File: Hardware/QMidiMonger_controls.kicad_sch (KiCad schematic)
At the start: 26 parts, among them J1 CV_Out, J10 Conn_01x04, J2 CV_Out, J20 Conn_01x09_Female, J21 Conn_01x08_Female, J22 Conn_01x08_Female, J23 Conn_01x03_Female, J3 CV_Out, J4 Gate_Out, J5 Gate_Out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

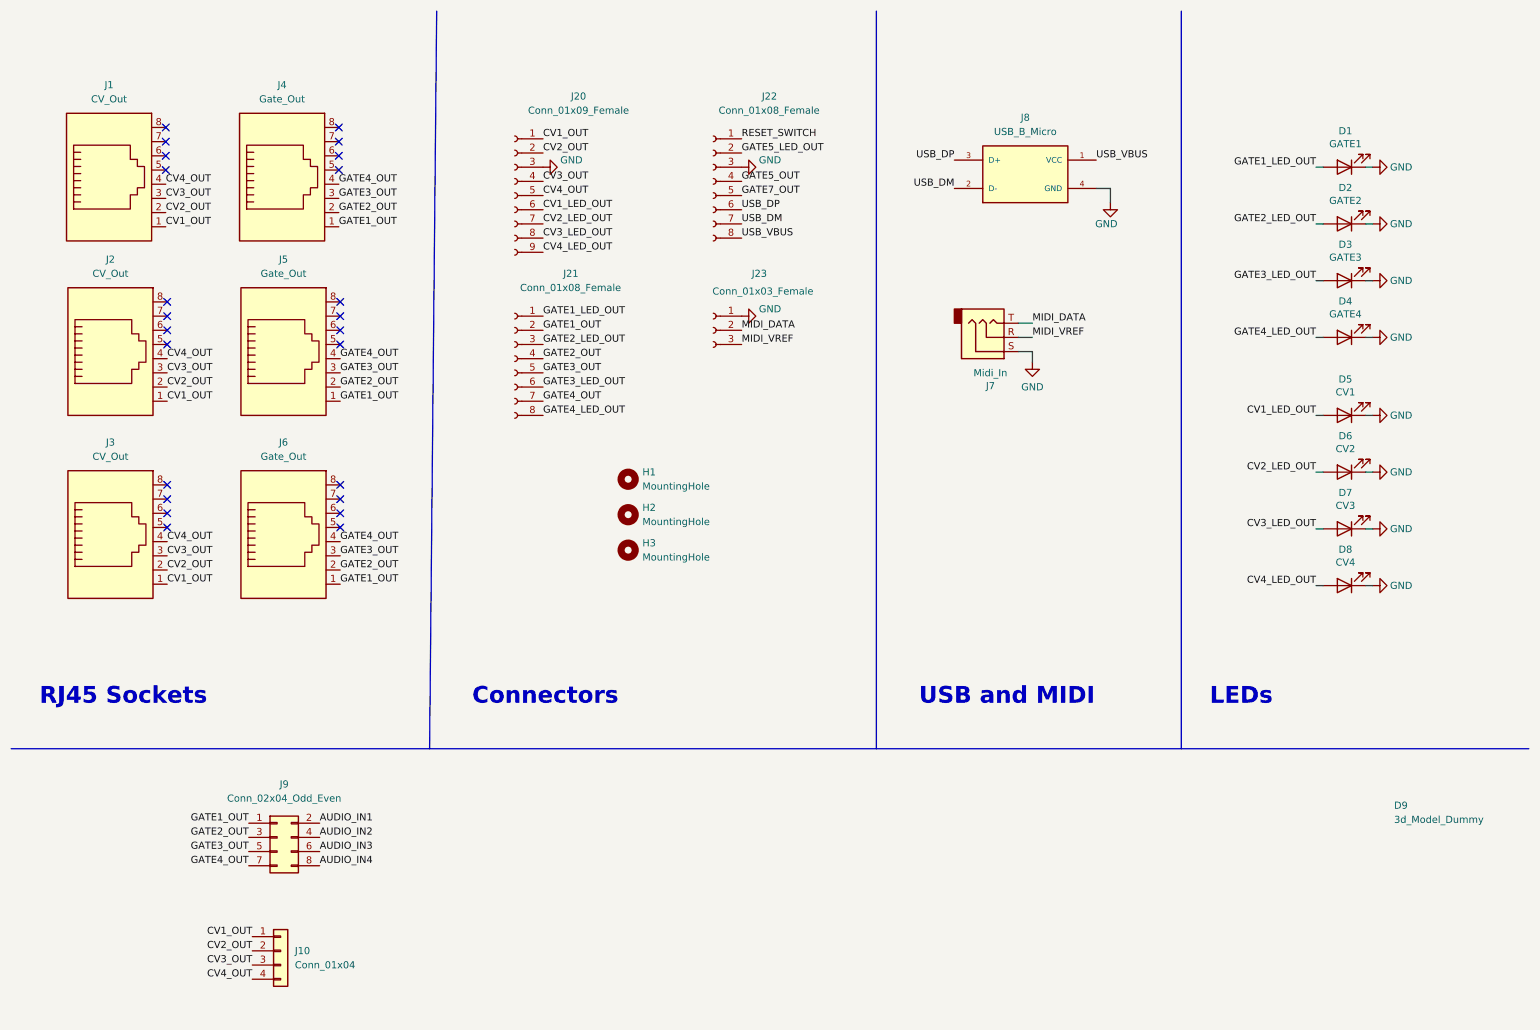
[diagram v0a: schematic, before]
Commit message: Added inter-board connector
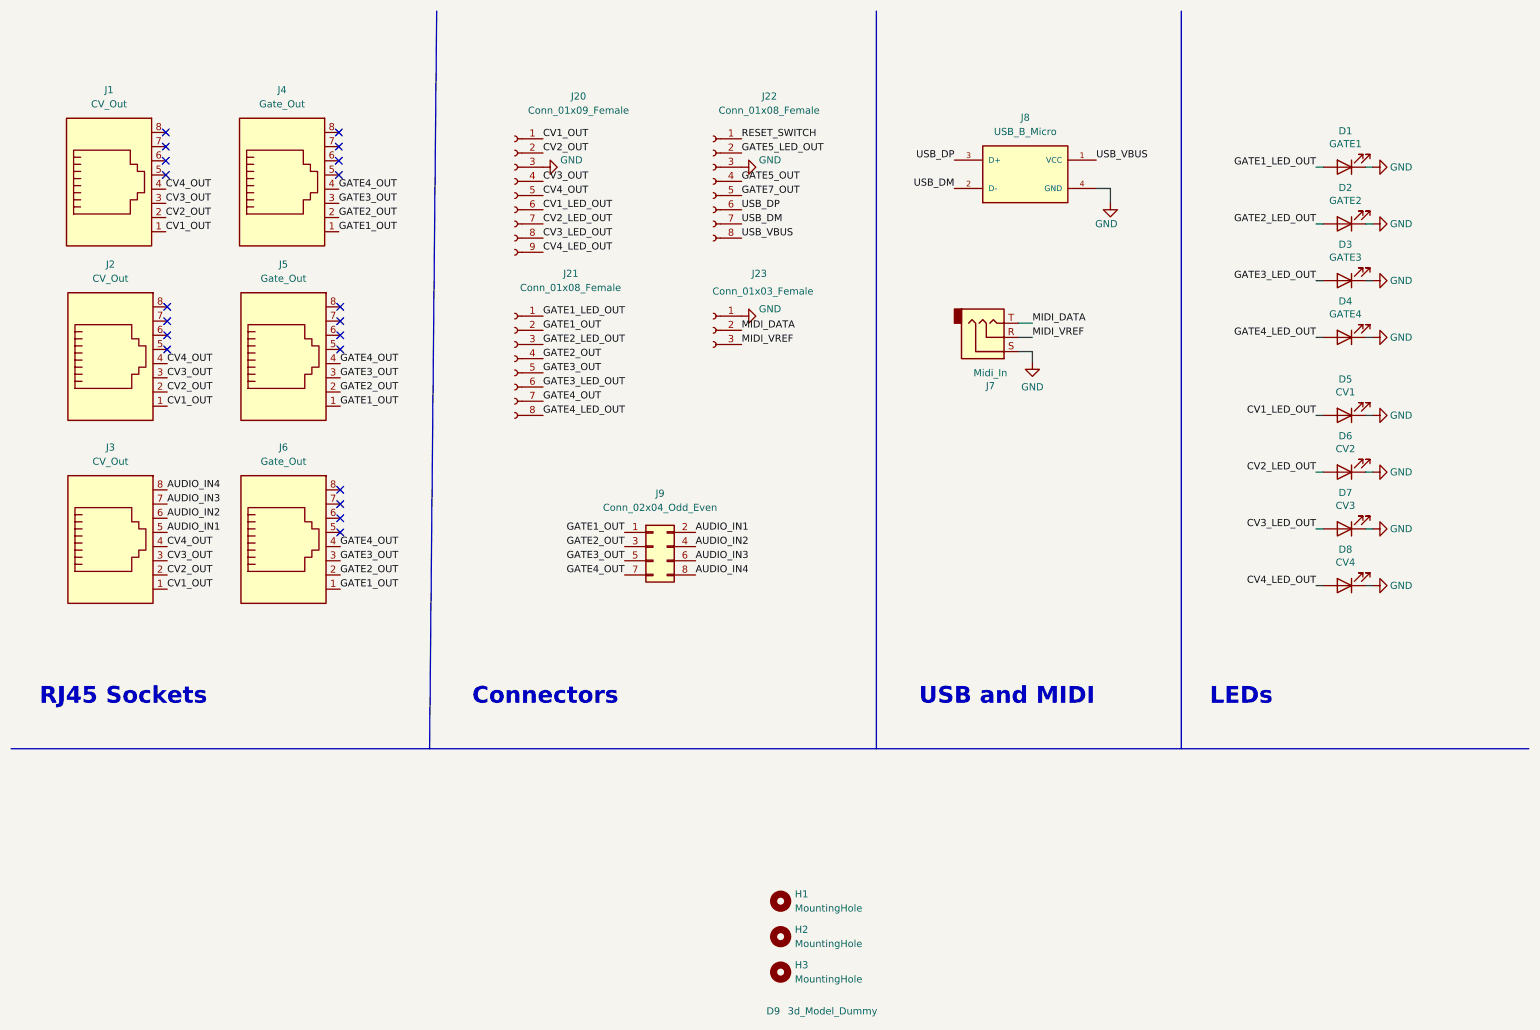
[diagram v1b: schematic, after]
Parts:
- removed J10: Conn_01x04, Connector_PinHeader_2.54mm:PinHeader_1x04_P2.54mm_Vertical, symbol Connector_Generic:Conn_01x04
- J23: footprint (none) -> Connector_PinHeader_2.54mm:PinHeader_1x03_P2.54mm_Vertical
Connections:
- net AUDIO_IN1: now also J3.5
- net AUDIO_IN2: now also J3.6
- net AUDIO_IN3: now also J3.7
- net AUDIO_IN4: now also J3.8
- no-connect marks 24 -> 20
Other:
- moved on the sheet: H1, H2, J1, J2, J3, J4, J5, J6, J9

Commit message: Cleaned up Panel and Controls
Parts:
- added H4: MountingHole, MountingHole:MountingHole_3.2mm_M3_ISO14580, symbol Mechanical:MountingHole
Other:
- moved on the sheet: H1, H2, H3
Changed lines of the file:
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@@
     (pin "1")
   )
-  (symbol (lib_id "Mechanical:MountingHole") (at 150.495 178.435 0) (unit 1)
-    (in_bom yes) (on_board yes) (fields_autoplaced)
-    (property "Reference" "H2" (id 0) (at 153.035 177.1649 0)
-      (effects (font (size 1.27 1.27)) (justify left))
-    )
-    (property "Value" "MountingHole" (id 1) (at 153.035 179.7049 0)
-      (effects (font (size 1.27 1.27)) (justify left))
-    )
-    (property "Footprint" "MountingHole:MountingHole_3.2mm_M3_ISO14580" (id 2) (at 150.495 178.435 0)
-      (effects (font (size 1.27 1.27)) hide)
-    )
-    (property "Datasheet" "~" (id 3) (at 150.495 178.435 0)
+  (symbol (lib_id "Mechanical:MountingHole") (at 151.13 176.53 0) (unit 1)
+    (in_bom yes) (on_board yes)
+    (property "Reference" "H2" (id 0) (at 153.67 176.53 0)
+      (effects (font (size 1.27 1.27)) (justify left))
+    )
+    (property "Value" "MountingHole" (id 1) (at 157.48 176.53 0)
+      (effects (font (size 1.27 1.27)) (justify left))
+    )
+    (property "Footprint" "MountingHole:MountingHole_3.2mm_M3_ISO14580" (id 2) (at 151.13 176.53 0)
+      (effects (font (size 1.27 1.27)) hide)
+    )
+    (property "Datasheet" "~" (id 3) (at 151.13 176.53 0)
       (effects (font (size 1.27 1.27)) hide)
     )
@@
     (pin "6")
   )
-  (symbol (lib_id "Mechanical:MountingHole") (at 150.495 184.785 0) (unit 1)
-    (in_bom yes) (on_board yes) (fields_autoplaced)
-    (property "Reference" "H3" (id 0) (at 153.035 183.5149 0)
-      (effects (font (size 1.27 1.27)) (justify left))
-    )
-    (property "Value" "MountingHole" (id 1) (at 153.035 186.0549 0)
-      (effects (font (size 1.27 1.27)) (justify left))
-    )
-    (property "Footprint" "MountingHole:MountingHole_3.2mm_M3_ISO14580" (id 2) (at 150.495 184.785 0)
-      (effects (font (size 1.27 1.27)) hide)
-    )
-    (property "Datasheet" "~" (id 3) (at 150.495 184.785 0)
+  (symbol (lib_id "Mechanical:MountingHole") (at 151.13 181.61 0) (unit 1)
+    (in_bom yes) (on_board yes)
+    (property "Reference" "H3" (id 0) (at 153.67 181.61 0)
+      (effects (font (size 1.27 1.27)) (justify left))
+    )
+    (property "Value" "MountingHole" (id 1) (at 157.48 181.61 0)
+      (effects (font (size 1.27 1.27)) (justify left))
+    )
+    (property "Footprint" "MountingHole:MountingHole_3.2mm_M3_ISO14580" (id 2) (at 151.13 181.61 0)
+      (effects (font (size 1.27 1.27)) hide)
+    )
+    (property "Datasheet" "~" (id 3) (at 151.13 181.61 0)
       (effects (font (size 1.27 1.27)) hide)
     )
@@
     (pin "8")
   )
+  (symbol (lib_id "Mechanical:MountingHole") (at 151.13 186.69 0) (unit 1)
+    (in_bom yes) (on_board yes)
+    (property "Reference" "H4" (id 0) (at 153.67 186.69 0)
+      (effects (font (size 1.27 1.27)) (justify left))
+    )
+    (property "Value" "MountingHole" (id 1) (at 157.48 186.69 0)
+      (effects (font (size 1.27 1.27)) (justify left))
+    )
+    (property "Footprint" "MountingHole:MountingHole_3.2mm_M3_ISO14580" (id 2) (at 151.13 186.69 0)
+      (effects (font (size 1.27 1.27)) hide)
+    )
+    (property "Datasheet" "~" (id 3) (at 151.13 186.69 0)
+      (effects (font (size 1.27 1.27)) hide)
+    )
+  )
   (symbol (lib_id "Connector:RJ45") (at 30.48 108.585 0) (unit 1)
     (in_bom yes) (on_board yes) (fields_autoplaced)
@@
     (pin "8")
   )
-  (symbol (lib_id "Mechanical:MountingHole") (at 150.495 172.085 0) (unit 1)
-    (in_bom yes) (on_board yes) (fields_autoplaced)
-    (property "Reference" "H1" (id 0) (at 153.035 170.8149 0)
-      (effects (font (size 1.27 1.27)) (justify left))
-    )
-    (property "Value" "MountingHole" (id 1) (at 153.035 173.3549 0)
-      (effects (font (size 1.27 1.27)) (justify left))
-    )
-    (property "Footprint" "MountingHole:MountingHole_3.2mm_M3_ISO14580" (id 2) (at 150.495 172.085 0)
-      (effects (font (size 1.27 1.27)) hide)
-    )
-    (property "Datasheet" "~" (id 3) (at 150.495 172.085 0)
+  (symbol (lib_id "Mechanical:MountingHole") (at 151.13 171.45 0) (unit 1)
+    (in_bom yes) (on_board yes)
+    (property "Reference" "H1" (id 0) (at 153.67 171.45 0)
+      (effects (font (size 1.27 1.27)) (justify left))
+    )
+    (property "Value" "MountingHole" (id 1) (at 157.48 171.45 0)
+      (effects (font (size 1.27 1.27)) (justify left))
+    )
+    (property "Footprint" "MountingHole:MountingHole_3.2mm_M3_ISO14580" (id 2) (at 151.13 171.45 0)
+      (effects (font (size 1.27 1.27)) hide)
+    )
+    (property "Datasheet" "~" (id 3) (at 151.13 171.45 0)
       (effects (font (size 1.27 1.27)) hide)
     )
@@
       (reference "H3") (unit 1) (value "MountingHole") (footprint "MountingHole:MountingHole_3.2mm_M3_ISO14580")
     )
+    (path "/9488fc83-dfc5-4711-97e2-a0787e6e6b10"
+      (reference "H4") (unit 1) (value "MountingHole") (footprint "MountingHole:MountingHole_3.2mm_M3_ISO14580")
+    )
     (path "/b97ad1b2-2d16-4fb2-ae0a-b795ae6e7172"
